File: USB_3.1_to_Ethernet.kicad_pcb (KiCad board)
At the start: 4 copper layers, 75 x 25 mm, 24 parts, among them J1 RJ45_JK0654219, J2 USB3_A, U1 LAN7801_9JX, U2 93LC56B_SN, U3 KSZ9031RNXCC, U4 TLV76733, U5 USBLC6-2P6, U6 TPS7A0212, Y1 25MHz, Y2 25MHz

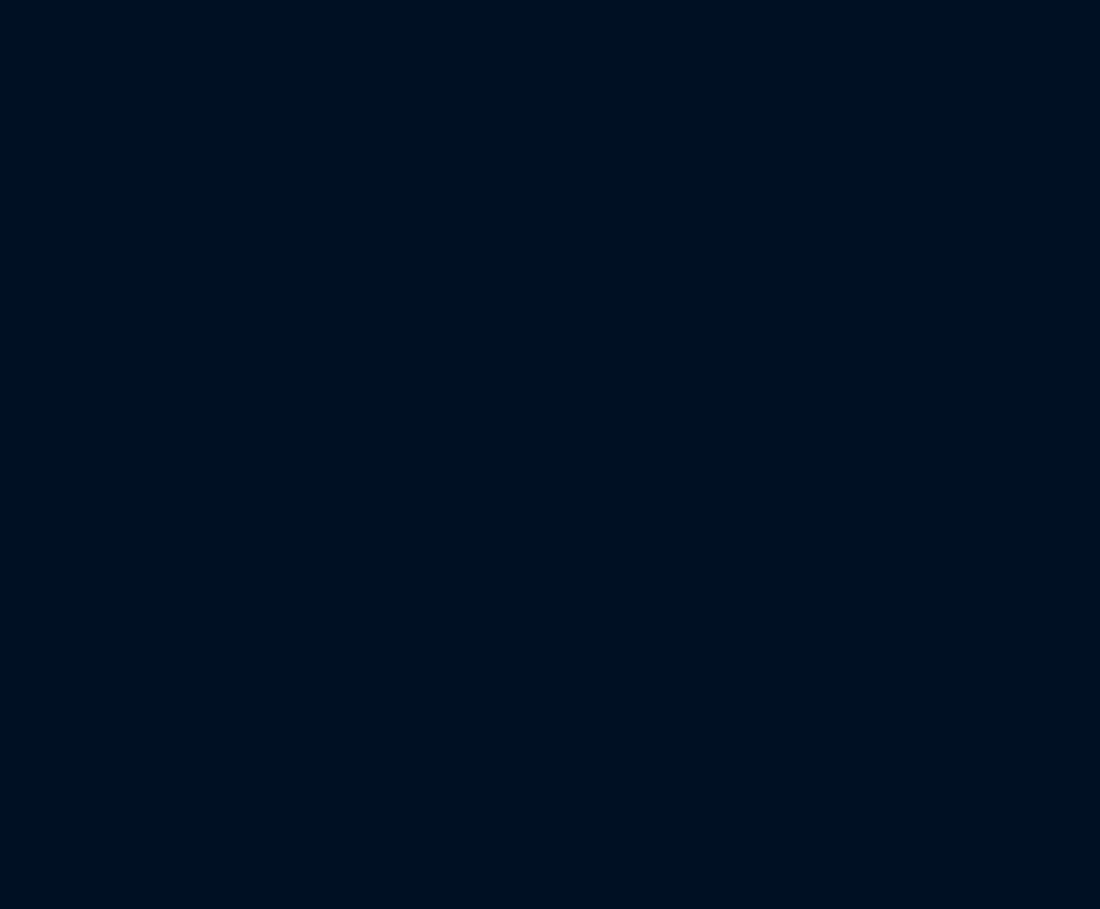
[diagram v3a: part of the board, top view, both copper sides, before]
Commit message: Added 27R resistors to RGMII interface, added 0.1uF AC coupling caps on sstx/rx, Magjack connections done
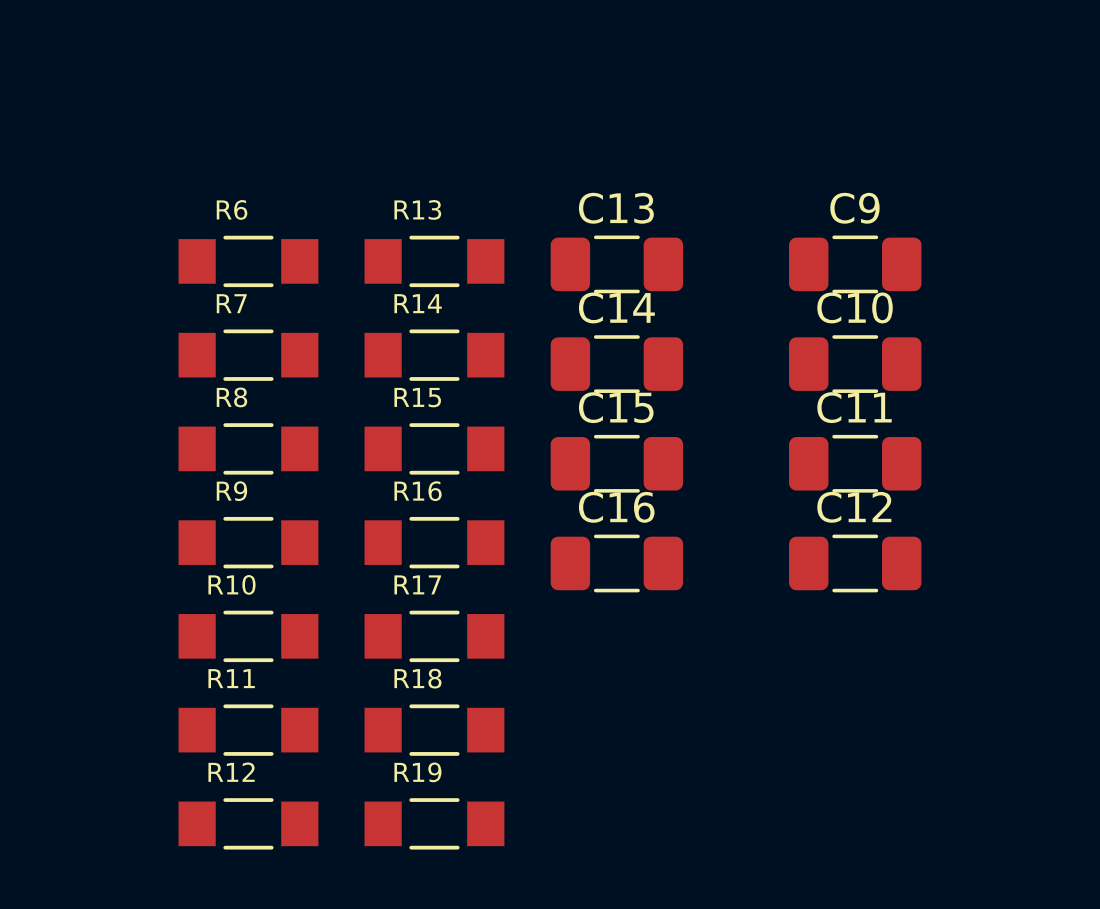
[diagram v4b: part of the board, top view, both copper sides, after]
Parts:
- added C10: 0.1uF, Capacitor_SMD:C_1206_3216Metric_Pad1.33x1.80mm_HandSolder, F.Cu at (123.5, 110.8)
- added C11: 0.1uF, Capacitor_SMD:C_1206_3216Metric_Pad1.33x1.80mm_HandSolder, F.Cu at (123.5, 114.2)
- added C12: 0.1uF, Capacitor_SMD:C_1206_3216Metric_Pad1.33x1.80mm_HandSolder, F.Cu at (123.5, 117.5)
- added C13: 0.1uF, Capacitor_SMD:C_1206_3216Metric_Pad1.33x1.80mm_HandSolder, F.Cu at (115.5, 107.5)
- added C14: 0.1uF, Capacitor_SMD:C_1206_3216Metric_Pad1.33x1.80mm_HandSolder, F.Cu at (115.5, 110.8)
- added C15: 0.1uF, Capacitor_SMD:C_1206_3216Metric_Pad1.33x1.80mm_HandSolder, F.Cu at (115.5, 114.2)
- added C16: 0.1uF, Capacitor_SMD:C_1206_3216Metric_Pad1.33x1.80mm_HandSolder, F.Cu at (115.5, 117.5)
- added C9: 0.1uF, Capacitor_SMD:C_1206_3216Metric_Pad1.33x1.80mm_HandSolder, F.Cu at (123.5, 107.5)
- added R10: 27R, Resistor_SMD:R_1206, F.Cu at (103.1, 120.0)
- added R11: 27R, Resistor_SMD:R_1206, F.Cu at (103.1, 123.1)
- added R12: 27R, Resistor_SMD:R_1206, F.Cu at (103.1, 126.2)
- added R13: 27R, Resistor_SMD:R_1206, F.Cu at (109.4, 107.3)
- added R14: 27R, Resistor_SMD:R_1206, F.Cu at (109.4, 110.5)
- added R15: 27R, Resistor_SMD:R_1206, F.Cu at (109.4, 113.7)
- added R16: 27R, Resistor_SMD:R_1206, F.Cu at (109.4, 116.8)
- added R17: 27R, Resistor_SMD:R_1206, F.Cu at (109.4, 120.0)
- added R18: 27R, Resistor_SMD:R_1206, F.Cu at (109.4, 123.1)
- added R19: 27R, Resistor_SMD:R_1206, F.Cu at (109.4, 126.2)
- added R6: 27R, Resistor_SMD:R_1206, F.Cu at (103.1, 107.3)
- added R7: 27R, Resistor_SMD:R_1206, F.Cu at (103.1, 110.5)
- added R8: 27R, Resistor_SMD:R_1206, F.Cu at (103.1, 113.7)
- added R9: 27R, Resistor_SMD:R_1206, F.Cu at (103.1, 116.8)
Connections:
- J1 pad 1: unconnected-(J1-MXCT3-Pad1) -> Net-(J1-MXCT3)
- J1 pad 10: unconnected-(J1-MX1--Pad10) -> /TXRXM_A
- J1 pad 11: unconnected-(J1-MX1+-Pad11) -> /TXRXP_A
- J1 pad 12: unconnected-(J1-MXCT1-Pad12) -> Net-(J1-MXCT1)
- J1 pad 13: unconnected-(J1-LED2--Pad13) -> /LED2-
- J1 pad 14: unconnected-(J1-LED2+-Pad14) -> 3v3_out
- J1 pad 15: unconnected-(J1-LED1--Pad15) -> /LED1-
- J1 pad 16: unconnected-(J1-LED1+-Pad16) -> 3v3_out
- J1 pad 2: unconnected-(J1-MX3--Pad2) -> /TXRXM_C
- J1 pad 3: unconnected-(J1-MX3+-Pad3) -> /TXRXP_C
- J1 pad 4: unconnected-(J1-MX2+-Pad4) -> /TXRXP_B
- J1 pad 5: unconnected-(J1-MX2--Pad5) -> /TXRXM_B
- J1 pad 6: unconnected-(J1-MXCT2-Pad6) -> Net-(J1-MXCT2)
- J1 pad 7: unconnected-(J1-MXCT4-Pad7) -> Net-(J1-MXCT4)
- J1 pad 8: unconnected-(J1-MX4+-Pad8) -> /TXRXP_D
- J1 pad 9: unconnected-(J1-MX4--Pad9) -> /TXRXM_D
- J1 pad SH: unconnected-(J1-PadSH) -> GND
- J2 pad 5: SSRX- -> Net-(J2-SSRX-)
- J2 pad 6: SSRX+ -> Net-(J2-SSRX+)
- J2 pad 8: SSTX- -> Net-(J2-SSTX-)
- J2 pad 9: SSTX+ -> Net-(J2-SSTX+)
- U3 pad 10: unconnected-(U3-TXRXP_D-Pad10) -> /TXRXP_D
- U3 pad 11: unconnected-(U3-TXRXM_D-Pad11) -> /TXRXM_D
- U3 pad 15: unconnected-(U3-LED2/PHYAD1-Pad15) -> /LED2/PHYAD1
- U3 pad 17: unconnected-(U3-LED1/PHYAD0/PME_N1-Pad17) -> /LED1/PHYAD0/PME_N1
- U3 pad 19: /RXD0 -> /TXD0
- U3 pad 2: unconnected-(U3-TXRXP_A-Pad2) -> /TXRXP_A
- U3 pad 20: /RXD1 -> /TXD1
- U3 pad 21: /RXD2 -> /TXD2
- U3 pad 22: /RXD3 -> /TXD3
- U3 pad 24: /TXC -> /GTX_CLK
- U3 pad 25: /TX_CTL -> /TX_EN
- U3 pad 27: /TXD3 -> /RXD3/MODE3
- U3 pad 28: /TXD2 -> /RXD2/MODE2
- U3 pad 3: unconnected-(U3-TXRXM_A-Pad3) -> /TXRXM_A
- U3 pad 31: /TXD1 -> /RXD1/MODE1
- U3 pad 32: /TXD0 -> /RXD0/MODE0
- U3 pad 33: /RX_CTL -> /RX_DV/CLK125_EN
- U3 pad 35: /RXC -> /RX_CLK/PHYAD2
- U3 pad 5: unconnected-(U3-TXRXP_B-Pad5) -> /TXRXP_B
- U3 pad 6: unconnected-(U3-TXRXM_B-Pad6) -> /TXRXM_B
- U3 pad 7: unconnected-(U3-TXRXP_C-Pad7) -> /TXRXP_C
- U3 pad 8: unconnected-(U3-TXRXM_C-Pad8) -> /TXRXM_C

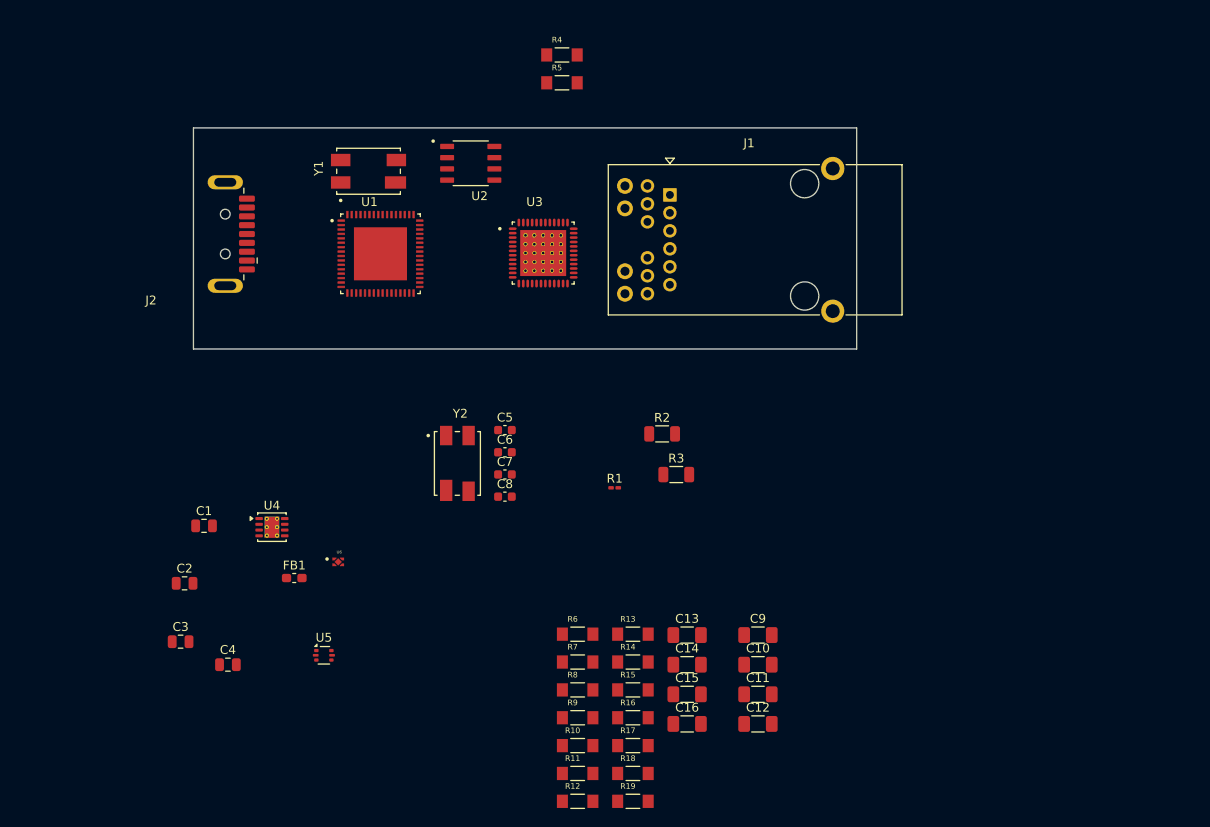
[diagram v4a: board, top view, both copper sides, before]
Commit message: 1. Layout placement started. placed Lan7801, PHY, EEPROM and regulators 2.changed D+ D- lines of USB-TVS diode reveresed for clean routing
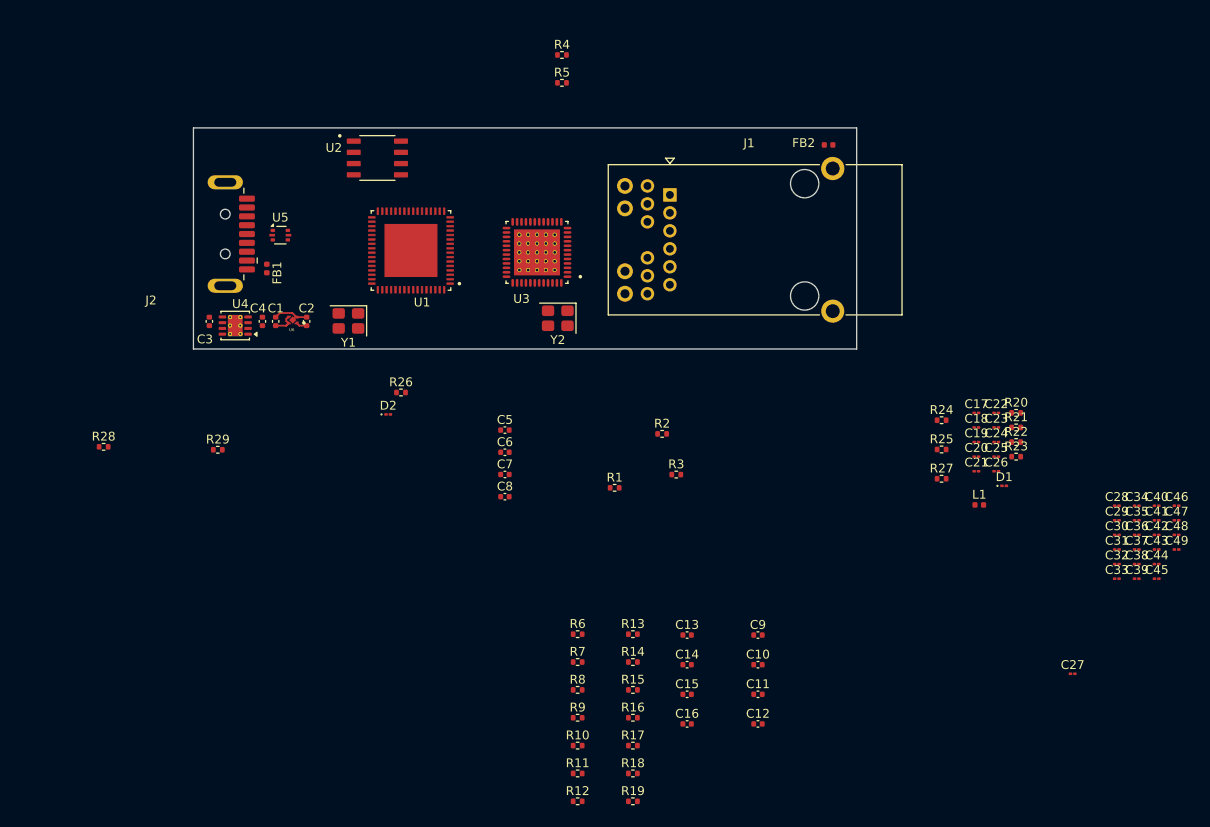
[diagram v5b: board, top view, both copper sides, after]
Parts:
- added C17: 0.1uF, Capacitor_SMD:C_01005_0402Metric, F.Cu at (148.2, 82.3)
- added C18: 0.1uF, Capacitor_SMD:C_01005_0402Metric, F.Cu at (148.2, 84.0)
- added C19: 0.1uF, Capacitor_SMD:C_01005_0402Metric, F.Cu at (148.2, 85.6)
- added C20: 0.1uF, Capacitor_SMD:C_01005_0402Metric, F.Cu at (148.2, 87.3)
- added C21: 0.1uF, Capacitor_SMD:C_01005_0402Metric, F.Cu at (148.2, 88.9)
- added C22: 0.1uF, Capacitor_SMD:C_01005_0402Metric, F.Cu at (150.5, 82.3)
- added C23: 0.1uF, Capacitor_SMD:C_01005_0402Metric, F.Cu at (150.5, 84.0)
- added C24: 0.1uF, Capacitor_SMD:C_01005_0402Metric, F.Cu at (150.5, 85.6)
- added C25: 22pF, Capacitor_SMD:C_01005_0402Metric, F.Cu at (150.5, 87.3)
- added C26: 1uF, Capacitor_SMD:C_01005_0402Metric, F.Cu at (150.5, 88.9)
- added C27: 4.7uF, Capacitor_SMD:C_01005_0402Metric, F.Cu at (159.1, 111.8)
- added C28: 4.7uF, Capacitor_SMD:C_01005_0402Metric, F.Cu at (164.1, 92.8)
- added C29: 0.1uF, Capacitor_SMD:C_01005_0402Metric, F.Cu at (164.1, 94.5)
- added C30: 0.1uF, Capacitor_SMD:C_01005_0402Metric, F.Cu at (164.1, 96.1)
- added C31: 0.1uF, Capacitor_SMD:C_01005_0402Metric, F.Cu at (164.1, 97.8)
- added C32: 0.1uF, Capacitor_SMD:C_01005_0402Metric, F.Cu at (164.1, 99.4)
- added C33: 0.1uF, Capacitor_SMD:C_01005_0402Metric, F.Cu at (164.1, 101.1)
- added C34: 0.1uF, Capacitor_SMD:C_01005_0402Metric, F.Cu at (166.4, 92.8)
- added C35: 0.1uF, Capacitor_SMD:C_01005_0402Metric, F.Cu at (166.4, 94.5)
- added C36: 0.1uF, Capacitor_SMD:C_01005_0402Metric, F.Cu at (166.4, 96.1)
- added C37: 0.1uF, Capacitor_SMD:C_01005_0402Metric, F.Cu at (166.4, 97.8)
- added C38: 0.1uF, Capacitor_SMD:C_01005_0402Metric, F.Cu at (166.4, 99.4)
- added C39: 0.1uF, Capacitor_SMD:C_01005_0402Metric, F.Cu at (166.4, 101.1)
- added C40: 0.1uF, Capacitor_SMD:C_01005_0402Metric, F.Cu at (168.6, 92.8)
- added C41: 0.1uF, Capacitor_SMD:C_01005_0402Metric, F.Cu at (168.6, 94.5)
- added C42: 0.1uF, Capacitor_SMD:C_01005_0402Metric, F.Cu at (168.6, 96.1)
- added C43: 0.1uF, Capacitor_SMD:C_01005_0402Metric, F.Cu at (168.6, 97.8)
- added C44: 0.1uF, Capacitor_SMD:C_01005_0402Metric, F.Cu at (168.6, 99.4)
- added C45: 0.1uF, Capacitor_SMD:C_01005_0402Metric, F.Cu at (168.6, 101.1)
- added C46: 0.1uF, Capacitor_SMD:C_01005_0402Metric, F.Cu at (170.9, 92.8)
- added C47: 0.1uF, Capacitor_SMD:C_01005_0402Metric, F.Cu at (170.9, 94.5)
- added C48: 0.1uF, Capacitor_SMD:C_01005_0402Metric, F.Cu at (170.9, 96.1)
- added C49: 0.1uF, Capacitor_SMD:C_01005_0402Metric, F.Cu at (170.9, 97.8)
- added D1: LED, LED_SMD:LED_01005_0402Metric, F.Cu at (151.4, 90.6)
- added D2: LED, LED_SMD:LED_01005_0402Metric, F.Cu at (81.7, 82.5)
- added FB2: FerriteBead_Small, Inductor_SMD:L_0402_1005Metric, F.Cu at (131.5, 52.0)
- added L1: 3.3uH, Inductor_SMD:L_0402_1005Metric, F.Cu at (148.6, 92.7)
- added R20: 2K, Resistor_SMD:R_0402_1005Metric, F.Cu at (152.7, 82.3)
- added R21: 10K, Resistor_SMD:R_0402_1005Metric, F.Cu at (152.7, 84.0)
- added R22: 10K, Resistor_SMD:R_0402_1005Metric, F.Cu at (152.7, 85.6)
- added R23: 12K, Resistor_SMD:R_0402_1005Metric, F.Cu at (152.7, 87.3)
- added R24: 1K, Resistor_SMD:R_0402_1005Metric, F.Cu at (144.3, 83.2)
- added R25: 1.5K, Resistor_SMD:R_0402_1005Metric, F.Cu at (144.3, 86.5)
- added R26: 4.7K, Resistor_SMD:R_0402_1005Metric, F.Cu at (83.2, 80.0)
- added R27: 4.7K, Resistor_SMD:R_0402_1005Metric, F.Cu at (144.3, 89.8)
- added R28: 4.7K, Resistor_SMD:R_0402_1005Metric, F.Cu at (49.5, 86.2)
- added R29: 4.7K, Resistor_SMD:R_0402_1005Metric, F.Cu at (62.5, 86.5)
- C1, C2, C3, C4: footprint Capacitor_SMD:C_0805_2012Metric -> Capacitor_SMD:C_0402_1005Metric
- C10, C11, C12, C13, C14, C15, C16, C9: footprint Capacitor_SMD:C_1206_3216Metric_Pad1.33x1.80mm_HandSolder -> Capacitor_SMD:C_0402_1005Metric
- C5, C6, C7, C8: footprint Capacitor_SMD:C_0603_1608Metric -> Capacitor_SMD:C_0402_1005Metric
- FB1: footprint Inductor_SMD:L_0603_1608Metric_Pad1.05x0.95mm_HandSolder -> Inductor_SMD:L_0402_1005Metric
- R1: footprint Resistor_SMD:R_0201_0603Metric_Pad0.64x0.40mm_HandSolder -> Resistor_SMD:R_0402_1005Metric
- R10, R11, R12, R13, R14, R15, R16, R17, R18, R19, R4, R5, R6, R7, R8, R9: footprint Resistor_SMD:R_1206 -> Resistor_SMD:R_0402_1005Metric
- R2, R3: footprint Resistor_SMD:R_1206_3216Metric -> Resistor_SMD:R_0402_1005Metric
- Y1, Y2: footprint Crystal:XTAL_ABMM325000MHZET -> Crystal:Crystal_SMD_3225-4Pin_3.2x2.5mm
- moved U5 47.8 mm to (69.5, 62.2)
- moved C4 39.0 mm to (67.5, 72.0), turned to 90 degrees
- moved C3 36.4 mm to (61.5, 72.0), turned to -90 degrees
- moved FB1 35.1 mm to (68.0, 66.0), turned to -90 degrees
- moved C2 32.7 mm to (72.5, 72.0), turned to 90 degrees
- moved U6 27.8 mm to (70.9, 71.8), turned to 180 degrees
- moved C1 24.5 mm to (69.0, 72.0), turned to 90 degrees
- moved U4 23.2 mm to (64.4, 72.5), turned to 180 degrees
- moved Y2 20.0 mm to (100.9, 71.6), turned to 180 degrees
- moved Y1 17.1 mm to (77.2, 71.9), turned to 180 degrees
- moved U2 10.6 mm to (80.5, 53.5)
- moved U1 3.47 mm to (84.3, 64.0), turned to 180 degrees
- moved U3 0.70 mm to (98.5, 64.2), turned to 180 degrees
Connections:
- C1 pad 1: +5V -> 3v3_out
- C11 pad 2: SSRX+ -> SSRX-
- C12 pad 2: SSRX- -> SSRX+
- J1 pad SH: GND -> GNDPWR
- J2 pad 2: Net-(J2-D-) -> /Power section/DP
- J2 pad 3: Net-(J2-D+) -> /Power section/DN
- U1 pad 1: unconnected-(U1-REF_REXT-Pad1) -> Net-(U1-REF_REXT)
- U1 pad 2: unconnected-(U1-REF_FILT-Pad2) -> Net-(U1-REF_FILT)
- U1 pad 20: unconnected-(U1-VDD12_SW_OUT-Pad20) -> Net-(U1-VDD12_SW_OUT)
- U1 pad 22: unconnected-(U1-VDD12_SW_FB-Pad22) -> Net-(U1-VDD12_SW_FB)
- U1 pad 28: VDD12CORE -> 1v2_core
- U1 pad 29: unconnected-(U1-VBUS_DET-Pad29) -> Net-(U1-VBUS_DET)
- U1 pad 30: unconnected-(U1-~{SUSPEND_N}-Pad30) -> /~{SUSPEND_N}
- U1 pad 31: unconnected-(U1-~{PHY_INT_N}-Pad31) -> /INT_N/PME_N2
- U1 pad 32: unconnected-(U1-~{PHY_RESET_N}-Pad32) -> /~{RESET_N}
- U1 pad 33: unconnected-(U1-DUPLEX-Pad33) -> Net-(U1-DUPLEX)
- U1 pad 36: unconnected-(U1-PME_MODE/GPIO5-Pad36) -> Net-(U1-PME_MODE/GPIO5)
- U1 pad 37: VDD12A -> 1v2_core
- U1 pad 42: VDD12A -> 1v2_core
- U1 pad 45: unconnected-(U1-~{PME_N}/GPIO6-Pad45) -> Net-(U1-~{PME_N}/GPIO6)
- U1 pad 46: unconnected-(U1-TEST-Pad46) -> Net-(U1-TEST)
- U1 pad 47: unconnected-(U1-~{RESET_N}/PME_CLEAR-Pad47) -> Net-(U1-~{RESET_N}/PME_CLEAR)
- U1 pad 54: VDD12CORE -> 1v2_core
- U1 pad 62: VDD12A -> 1v2_core
- U1 pad 63: unconnected-(U1-VDD25_REG_OUT-Pad63) -> Net-(U1-VDD25_REG_OUT)
- U3 pad 38: unconnected-(U3-INT_N/PME_N2-Pad38) -> /INT_N/PME_N2
- U3 pad 42: unconnected-(U3-~{RESET_N}-Pad42) -> /~{RESET_N}
- U3 pad 44: unconnected-(U3-AVDDL_PLL-Pad44) -> 1v2_core
- U3 pad 48: unconnected-(U3-ISET-Pad48) -> Net-(U3-ISET)
- U5 pad 1: Net-(J2-D-) -> /Power section/DN
- U5 pad 3: Net-(J2-D+) -> /Power section/DP
- U6 pad 3: +5V -> 3v3_out
- U6 pad 4: +5V -> 3v3_out
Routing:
- net GND: track 0.00 -> 4.45 mm
- net 3v3_out: track 0.00 -> 2.84 mm
- net 1v2_core: track 0.00 -> 1.20 mm

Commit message: merged with main branch, no major change in pcb or schematics
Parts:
- moved C10 69.6 mm to (69.8, 66.5)
- moved C9 69.1 mm to (69.8, 64.1)
- moved R4 34.3 mm to (73.3, 61.7)
- moved R5 33.3 mm to (73.4, 63.0)
- moved R26 7.55 mm to (76.9, 84.2)
- moved D2 6.26 mm to (77.7, 87.3)
- moved Y1 4.32 mm to (81.5, 71.5), turned to 0 degrees
- moved FB1 1.97 mm to (69.8, 65.2), turned to 0 degrees
- moved C1 0.26 mm to (68.9, 72.2)
- moved C2 0.26 mm to (72.4, 72.2)
- moved C3 0.26 mm to (61.4, 72.2)
- moved C4 0.26 mm to (67.4, 72.2)
- moved U4 0.26 mm to (64.3, 72.7)
- moved U6 0.26 mm to (70.9, 72.1)
- moved U5 0.21 mm to (69.7, 62.2)
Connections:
- net Net-(J2-SSRX+) renamed /Power section/ssrx_P
- net Net-(J2-SSRX-) renamed /Power section/ssrx_N
- net Net-(J2-SSTX+) renamed /Power section/sstx_P
- net Net-(J2-SSTX-) renamed /Power section/sstx_N
- C11 pad 2: SSRX- -> SSRX+
- C12 pad 2: SSRX+ -> SSRX-
